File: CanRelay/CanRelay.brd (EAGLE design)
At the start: 84.6 x 65.5 mm, 20 parts

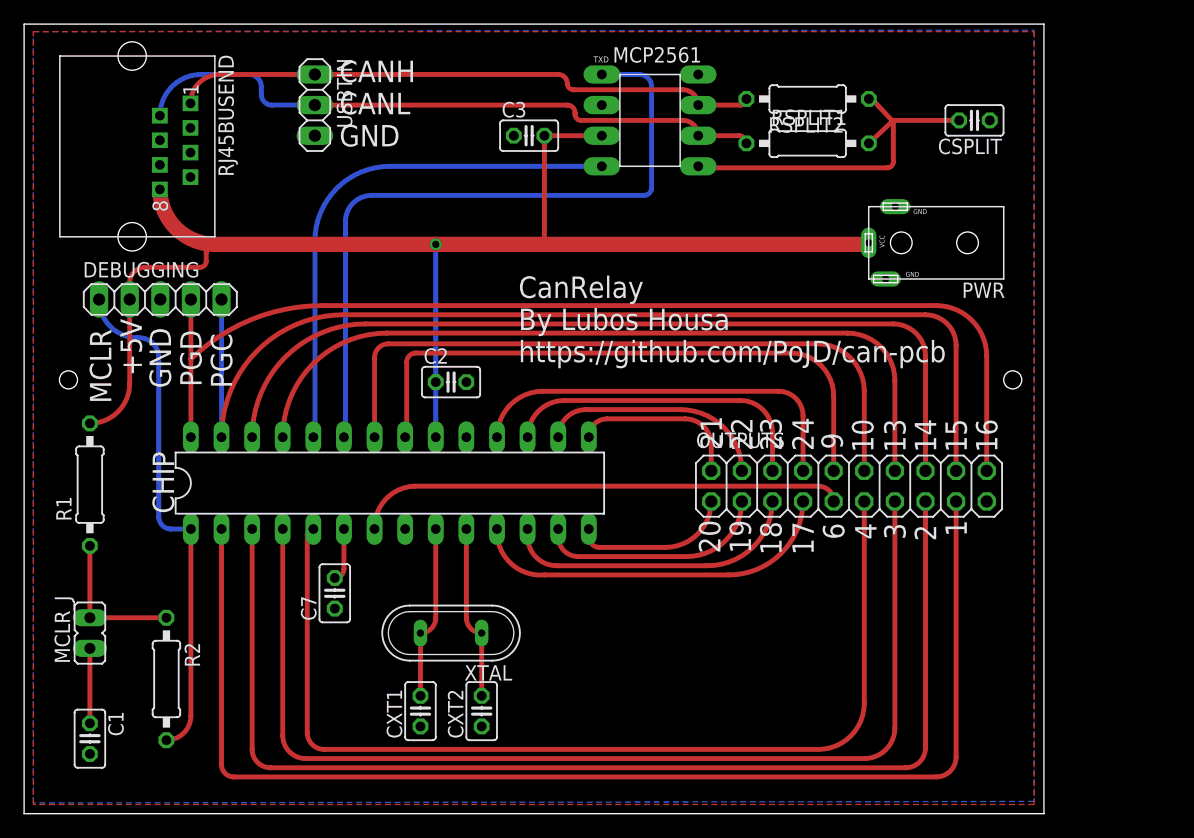
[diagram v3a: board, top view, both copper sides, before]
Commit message: final tuning of both boards - squeezing switch board a bit yet, adding some more silkscreen, exporting to image to share on some electrical forums for checks
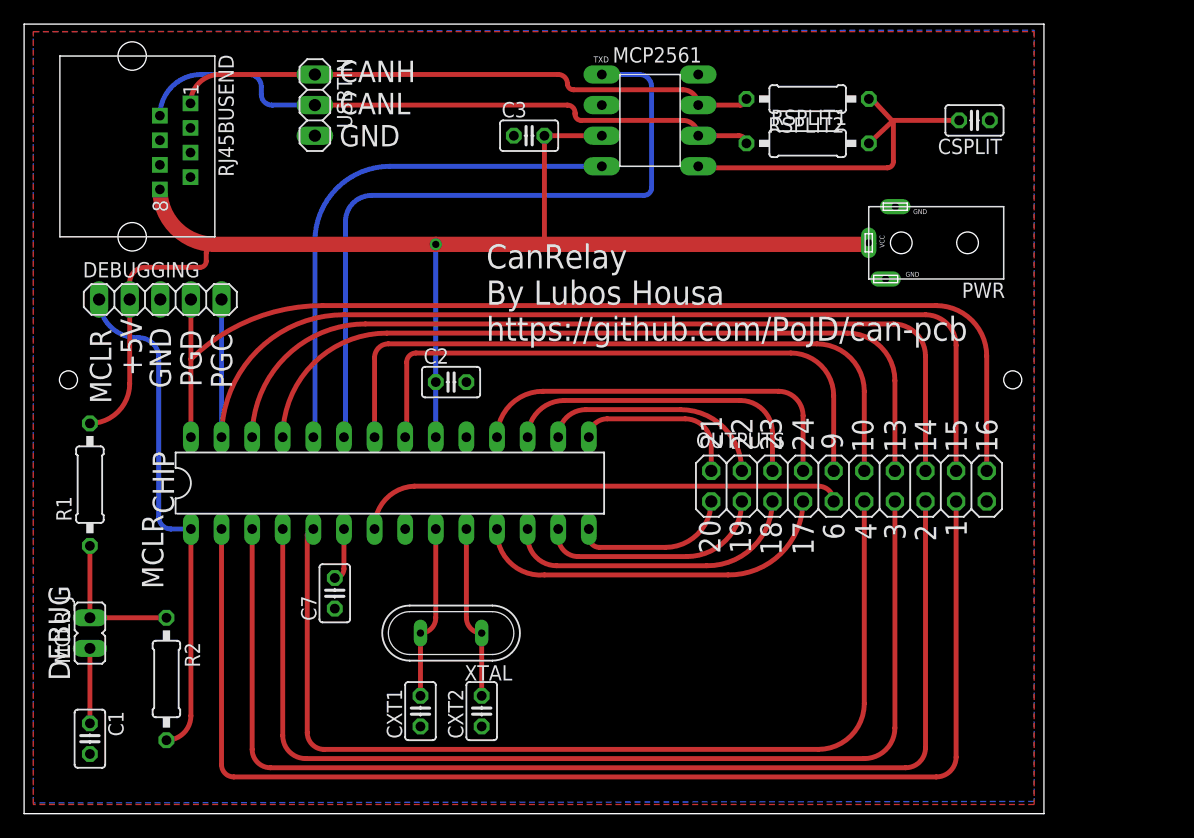
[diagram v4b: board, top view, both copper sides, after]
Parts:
- PWR: value DC-JACK-GK0.65SMALL -> DC-JACK-GK0.65S
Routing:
- added copper zone on layer 16, net GND
- removed copper zone on layer 16, net N$3
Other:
- board text added: "DEBUG"
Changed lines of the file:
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@@
 <layer number="27" name="tValues" color="7" fill="1" visible="yes" active="yes"/>
 <layer number="28" name="bValues" color="7" fill="1" visible="yes" active="yes"/>
-<layer number="29" name="tStop" color="7" fill="3" visible="no" active="yes"/>
-<layer number="30" name="bStop" color="7" fill="6" visible="no" active="yes"/>
-<layer number="31" name="tCream" color="7" fill="4" visible="no" active="yes"/>
-<layer number="32" name="bCream" color="7" fill="5" visible="no" active="yes"/>
-<layer number="33" name="tFinish" color="6" fill="3" visible="no" active="yes"/>
-<layer number="34" name="bFinish" color="6" fill="6" visible="no" active="yes"/>
-<layer number="35" name="tGlue" color="7" fill="4" visible="no" active="yes"/>
-<layer number="36" name="bGlue" color="7" fill="5" visible="no" active="yes"/>
-<layer number="37" name="tTest" color="7" fill="1" visible="no" active="yes"/>
-<layer number="38" name="bTest" color="7" fill="1" visible="no" active="yes"/>
+<layer number="29" name="tStop" color="7" fill="3" visible="yes" active="yes"/>
+<layer number="30" name="bStop" color="7" fill="6" visible="yes" active="yes"/>
+<layer number="31" name="tCream" color="7" fill="4" visible="yes" active="yes"/>
+<layer number="32" name="bCream" color="7" fill="5" visible="yes" active="yes"/>
+<layer number="33" name="tFinish" color="6" fill="3" visible="yes" active="yes"/>
+<layer number="34" name="bFinish" color="6" fill="6" visible="yes" active="yes"/>
+<layer number="35" name="tGlue" color="7" fill="4" visible="yes" active="yes"/>
+<layer number="36" name="bGlue" color="7" fill="5" visible="yes" active="yes"/>
+<layer number="37" name="tTest" color="7" fill="1" visible="yes" active="yes"/>
+<layer number="38" name="bTest" color="7" fill="1" visible="yes" active="yes"/>
 <layer number="39" name="tKeepout" color="4" fill="11" visible="yes" active="yes"/>
 <layer number="40" name="bKeepout" color="1" fill="11" visible="yes" active="yes"/>
@@
 <layer number="42" name="bRestrict" color="1" fill="10" visible="yes" active="yes"/>
 <layer number="43" name="vRestrict" color="2" fill="10" visible="yes" active="yes"/>
-<layer number="44" name="Drills" color="7" fill="1" visible="no" active="yes"/>
+<layer number="44" name="Drills" color="7" fill="1" visible="yes" active="yes"/>
 <layer number="45" name="Holes" color="7" fill="1" visible="yes" active="yes"/>
-<layer number="46" name="Milling" color="3" fill="1" visible="no" active="yes"/>
-<layer number="47" name="Measures" color="7" fill="1" visible="no" active="yes"/>
+<layer number="46" name="Milling" color="3" fill="1" visible="yes" active="yes"/>
+<layer number="47" name="Measures" color="7" fill="1" visible="yes" active="yes"/>
 <layer number="48" name="Document" color="7" fill="1" visible="yes" active="yes"/>
 <layer number="49" name="Reference" color="7" fill="1" visible="yes" active="yes"/>
@@
 <wire x1="84.633" y1="65.522" x2="0" y2="65.522" width="0" layer="20"/>
 <wire x1="0" y1="65.522" x2="0" y2="0" width="0" layer="20"/>
-<text x="41.021" y="37.465" size="1.778" layer="21">CanRelay
+<text x="38.354" y="39.243" size="2" layer="21">CanRelay
 By Lubos Housa
 https://github.com/PoJD/can-pcb</text>
@@
 <text x="75.692" y="22.606" size="1.778" layer="21" rot="R90">2</text>
 <text x="78.232" y="22.987" size="1.778" layer="21" rot="R90">1</text>
+<text x="11.557" y="18.669" size="1.778" layer="21" rot="R90">MCLR</text>
+<text x="3.81" y="11.049" size="1.778" layer="21" rot="R90">DEBUG</text>
 </plain>
 <attributes>
@@
 </class>
 </classes>
-<designrules name="default">
+<designrules name="default *">
 <description language="de">&lt;b&gt;EAGLE Design Rules&lt;/b&gt;
 &lt;p&gt;
@@
 <param name="mvStopFrame" value="1"/>
 <param name="mvCreamFrame" value="0"/>
-<param name="mlMinStopFrame" value="4mil"/>
+<param name="mlMinStopFrame" value="2mil"/>
 <param name="mlMaxStopFrame" value="4mil"/>
 <param name="mlMinCreamFrame" value="0mil"/>
@@
 <element name="MCP2561" library="PoJD" package="MCP2561_PDIP" value="MCP2561MCP" x="51.943" y="57.531"/>
 <element name="OUTPUTS" library="pinhead" package="2X10" value="" x="68.453" y="27.178"/>
-<element name="PWR" library="PoJD" package="DC-JACK-GK0.65" value="DC-JACK-GK0.65SMALL" x="75.692" y="47.371" rot="R180"/>
+<element name="PWR" library="PoJD" package="DC-JACK-GK0.65" value="DC-JACK-GK0.65S" x="75.692" y="47.371" rot="R180"/>
 <element name="R1" library="rcl" package="0207/10" value="10000" x="5.461" y="27.305" rot="R90"/>
 <element name="R2" library="rcl" package="0207/10" value="470" x="11.811" y="11.176" rot="R270"/>
@@
 <contactref element="PWR" pad="GND1"/>
 <contactref element="PWR" pad="GND2"/>
-<polygon width="0.254" layer="1">
+<polygon width="0.4064" layer="1" isolate="0.4064">
 <vertex x="0.762" y="64.897"/>
 <vertex x="83.82" y="64.897"/>
@@
 </polygon>
 <contactref element="USBTIN" pad="3"/>
+<polygon width="0.4064" layer="16" isolate="0.4064">
+<vertex x="0.762" y="64.897"/>
+<vertex x="83.82" y="65.024"/>
+<vertex x="83.82" y="1.016"/>
+<vertex x="0.762" y="0.889"/>
+</polygon>
 </signal>
 <signal name="N$2">
@@
 <wire x1="46.863" y1="22.987" x2="46.863" y2="23.622" width="0.4064" layer="1"/>
 </signal>
-<signal name="N$3">
-<polygon width="0.254" layer="16">
-<vertex x="0.762" y="64.897"/>
-<vertex x="83.82" y="65.024"/>
-<vertex x="83.82" y="1.016"/>
-<vertex x="0.762" y="0.889"/>
-</polygon>
-</signal>
 </signals>

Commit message: incorporated hints from web: set proper sizes for caps, left enough space for them to be bend on the board. Reviewed any acute angles in traces. Increased isolation in ground copper so that no so called GND fingers are in the PCB Relay board. Also double checked other footprints, XTAL is a bit larger than real, but not by much
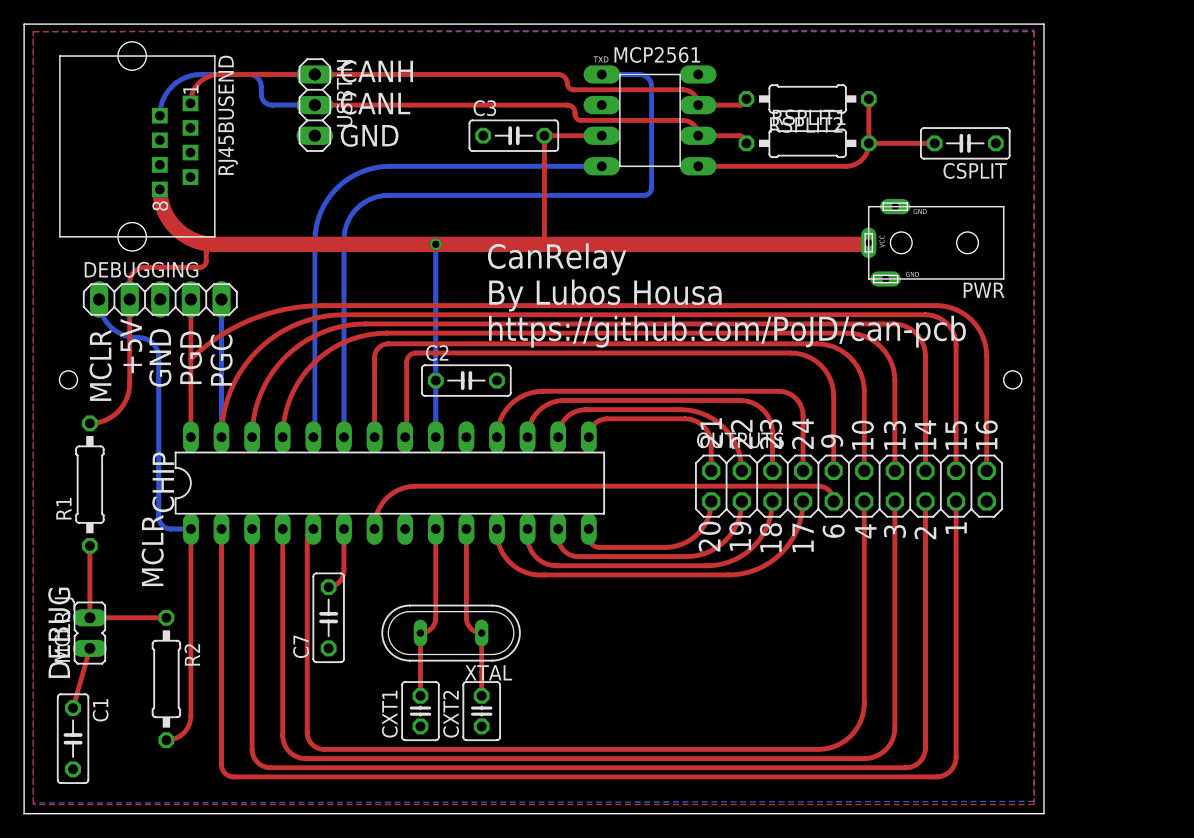
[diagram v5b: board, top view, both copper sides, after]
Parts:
- C1, C2, C3, C7, CSPLIT: device rcl:C025-025X050 -> rcl:C050-025X075
- CXT1, CXT2: device rcl:C025-025X050 -> rcl:C025-030X050
- RSPLIT1, RSPLIT2: value 56 -> 50
- moved C7 2.09 mm to (25.3, 16.3)
- moved CSPLIT 2.05 mm to (78.1, 55.6)
- moved C1 1.40 mm to (4.06, 6.22)
- moved C2 1.28 mm to (36.7, 35.9)
- moved C3 1.27 mm to (40.6, 56.3)
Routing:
- net SPLIT: track 30.9 -> 24.3 mm
- net N$1: track 6.22 -> 5.15 mm
- net N$4: track 4.38 -> 5.29 mm
- net TXD: track 57.4 -> 56.8 mm
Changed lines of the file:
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@@
 </autorouter>
 <elements>
-<element name="C1" library="rcl" package="C025-025X050" value="0.1uF" x="5.461" y="6.223" rot="R270"/>
-<element name="C2" library="rcl" package="C025-025X050" value="0.1uF" x="35.433" y="35.814"/>
-<element name="C3" library="rcl" package="C025-025X050" value="0.1uF" x="41.91" y="56.261"/>
-<element name="C7" library="rcl" package="C025-025X050" value="10 uF" x="25.781" y="18.288" rot="R90"/>
+<element name="C1" library="rcl" package="C050-025X075" value="0.1uF" x="4.064" y="6.223" rot="R270"/>
+<element name="C2" library="rcl" package="C050-025X075" value="0.1uF" x="36.703" y="35.941"/>
+<element name="C3" library="rcl" package="C050-025X075" value="0.1uF" x="40.64" y="56.261"/>
+<element name="C7" library="rcl" package="C050-025X075" value="10 uF" x="25.273" y="16.256" rot="R90"/>
 <element name="CHIP" library="microchip" package="DIL28-3" value="PIC18F2480-I/SP" x="30.353" y="27.432">
 <attribute name="OC_FARNELL" value="9321217" x="30.353" y="27.432" size="1.778" layer="27" display="off"/>
@@
 <attribute name="MPN" value="PIC18F2480-I/SP" x="30.353" y="27.432" size="1.778" layer="27" display="off"/>
 </element>
-<element name="CSPLIT" library="rcl" package="C025-025X050" value="4.7nF" x="78.867" y="57.531" rot="R180"/>
-<element name="CXT1" library="rcl" package="C025-025X050" value="33pF" x="32.893" y="8.509" rot="R90"/>
-<element name="CXT2" library="rcl" package="C025-025X050" value="33pF" x="37.973" y="8.509" rot="R90"/>
+<element name="CSPLIT" library="rcl" package="C050-025X075" value="4.7nF" x="78.105" y="55.626" rot="R180"/>
+<element name="CXT1" library="rcl" package="C025-030X050" value="33pF" x="32.893" y="8.509" rot="R90"/>
+<element name="CXT2" library="rcl" package="C025-030X050" value="33pF" x="37.973" y="8.509" rot="R90"/>
 <element name="DEBUGGING" library="pinhead" package="1X05" value="" x="11.303" y="42.672"/>
 <element name="MCLR_J" library="jumper" package="JP1" value="" x="5.461" y="14.986"/>
@@
 <element name="R2" library="rcl" package="0207/10" value="470" x="11.811" y="11.176" rot="R270"/>
 <element name="RJ45BUSEND" library="PoJD" package="WEBP88_RJ45_SINGLE" value="WEBP88_SSINGLE" x="9.398" y="55.372" rot="R270"/>
-<element name="RSPLIT1" library="rcl" package="0207/10" value="56" x="65.024" y="55.626"/>
-<element name="RSPLIT2" library="rcl" package="0207/10" value="56" x="65.024" y="59.309" rot="R180"/>
+<element name="RSPLIT1" library="rcl" package="0207/10" value="50" x="65.024" y="55.626"/>
+<element name="RSPLIT2" library="rcl" package="0207/10" value="50" x="65.024" y="59.309" rot="R180"/>
 <element name="XTAL" library="special" package="QS" value="16MHz" x="35.433" y="14.986" rot="R180"/>
 <element name="USBTIN" library="pinhead" package="1X03" value="" x="24.13" y="58.801" rot="R270"/>
@@
 <wire x1="8.763" y1="35.687" x2="8.763" y2="42.672" width="0.4064" layer="1"/>
 <via x="34.163" y="47.244" extent="1-16" drill="0.6" shape="square"/>
-<wire x1="34.163" y1="47.244" x2="34.163" y2="35.814" width="0.4064" layer="16"/>
-<wire x1="34.163" y1="35.814" x2="34.163" y2="31.242" width="0.4064" layer="16"/>
+<wire x1="34.163" y1="47.244" x2="34.163" y2="35.941" width="0.4064" layer="16"/>
+<wire x1="34.163" y1="35.941" x2="34.163" y2="31.242" width="0.4064" layer="16"/>
 <wire x1="43.18" y1="56.261" x2="43.18" y2="47.244" width="0.4064" layer="1"/>
 <wire x1="34.163" y1="47.244" x2="15.826" y2="47.244" width="1.27" layer="1"/>
@@
 <contactref element="PWR" pad="GND1"/>
 <contactref element="PWR" pad="GND2"/>
-<polygon width="0.4064" layer="1" isolate="0.4064">
+<polygon width="0.4064" layer="1" isolate="0.8128">
 <vertex x="0.762" y="64.897"/>
 <vertex x="83.82" y="64.897"/>
@@
 </polygon>
 <contactref element="USBTIN" pad="3"/>
-<polygon width="0.4064" layer="16" isolate="0.4064">
+<polygon width="0.4064" layer="16" isolate="0.8128">
 <vertex x="0.762" y="64.897"/>
 <vertex x="83.82" y="65.024"/>
@@
 <contactref element="C1" pad="1"/>
 <contactref element="MCLR_J" pad="1"/>
-<wire x1="5.461" y1="7.493" x2="5.461" y2="13.716" width="0.4064" layer="1"/>
+<wire x1="4.064" y1="8.763" x2="5.461" y2="13.716" width="0.4064" layer="1"/>
 </signal>
 <signal name="N$4">
 <contactref element="CHIP" pad="6"/>
 <contactref element="C7" pad="2"/>
-<wire x1="25.781" y1="19.558" x2="26.543" y2="20.32" width="0.4064" layer="1" curve="90"/>
+<wire x1="25.273" y1="18.796" x2="26.543" y2="20.32" width="0.4064" layer="1" curve="90"/>
 <wire x1="26.543" y1="20.32" x2="26.543" y2="23.622" width="0.4064" layer="1"/>
 </signal>
@@
 <contactref element="CHIP" pad="23"/>
 <wire x1="26.543" y1="31.242" x2="26.67" y2="31.369" width="0.4064" layer="16" curve="90"/>
-<wire x1="26.67" y1="31.369" x2="26.67" y2="49.149" width="0.4064" layer="16"/>
-<wire x1="26.67" y1="49.149" x2="28.829" y2="51.308" width="0.4064" layer="16" curve="-90"/>
-<wire x1="28.829" y1="51.308" x2="51.435" y2="51.308" width="0.4064" layer="16"/>
 <wire x1="51.435" y1="51.308" x2="52.07" y2="51.943" width="0.4064" layer="16" curve="90"/>
 <wire x1="52.07" y1="51.943" x2="52.07" y2="60.325" width="0.4064" layer="16"/>
 <wire x1="52.07" y1="60.325" x2="51.054" y2="61.341" width="0.4064" layer="16" curve="90"/>
 <wire x1="51.054" y1="61.341" x2="47.943" y2="61.341" width="0.4064" layer="16"/>
+<wire x1="51.435" y1="51.308" x2="30.226" y2="51.308" width="0.4064" layer="16"/>
+<wire x1="30.226" y1="51.308" x2="26.543" y2="47.625" width="0.4064" layer="16" curve="90"/>
+<wire x1="26.543" y1="47.625" x2="26.543" y2="31.242" width="0.4064" layer="16"/>
 </signal>
 <signal name="RXD">
@@
 <contactref element="RSPLIT1" pad="2"/>
 <contactref element="CSPLIT" pad="2"/>
-<wire x1="77.597" y1="57.531" x2="72.136" y2="57.531" width="0.4064" layer="1"/>
-<wire x1="55.943" y1="53.721" x2="56.07" y2="53.594" width="0.4064" layer="1" curve="90"/>
-<wire x1="56.07" y1="53.594" x2="71.628" y2="53.594" width="0.4064" layer="1"/>
-<wire x1="71.628" y1="53.594" x2="72.136" y2="54.102" width="0.4064" layer="1" curve="90"/>
-<wire x1="72.136" y1="54.102" x2="72.136" y2="57.531" width="0.4064" layer="1"/>
 <wire x1="70.358" y1="59.309" x2="70.104" y2="59.309" width="0.4064" layer="1"/>
-<wire x1="72.009" y1="57.531" x2="72.136" y2="57.531" width="0.4064" layer="1"/>
-<wire x1="70.358" y1="59.309" x2="72.009" y2="57.531" width="0.4064" layer="1"/>
-<wire x1="70.104" y1="55.626" x2="72.136" y2="57.531" width="0.4064" layer="1"/>
+<wire x1="70.104" y1="59.309" x2="70.104" y2="55.626" width="0.4064" layer="1"/>
+<wire x1="70.104" y1="55.626" x2="75.565" y2="55.626" width="0.4064" layer="1"/>
+<wire x1="70.104" y1="55.626" x2="68.199" y2="53.721" width="0.4064" layer="1" curve="-90"/>
+<wire x1="68.199" y1="53.721" x2="55.943" y2="53.721" width="0.4064" layer="1"/>
 </signal>
 <signal name="PGC/O15">
